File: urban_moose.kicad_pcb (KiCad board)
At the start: 2 copper layers, 27.4 x 49.5 mm, 52 parts, among them P1 SWD, P2 EXT, P3 ANT, Q1 MOSFET_N, Q2 MOSFET_N, SW1 SW_PUSH, U1 nRF51822-QFAA, U2 DS18B20, U3 BMP180, U4 Si1145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

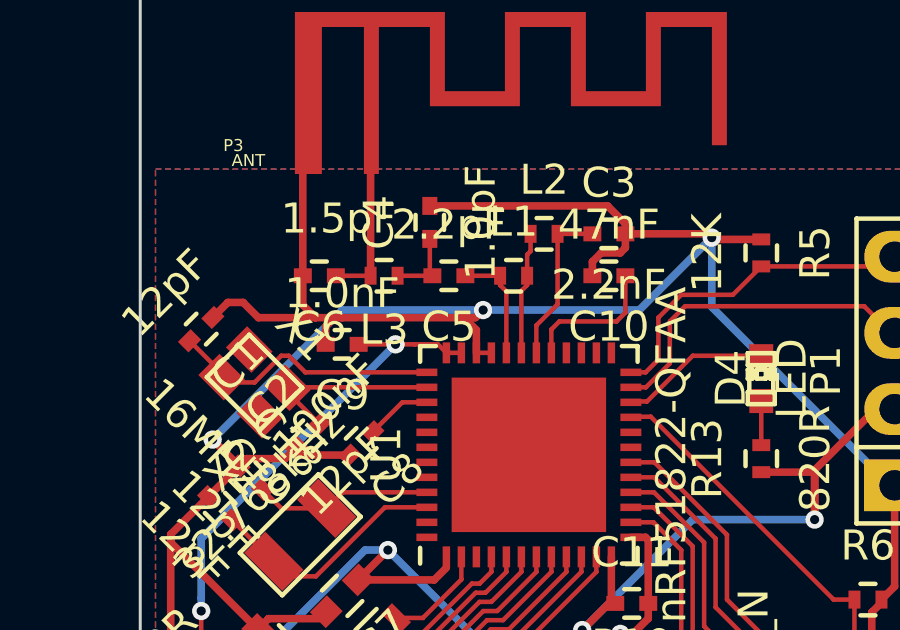
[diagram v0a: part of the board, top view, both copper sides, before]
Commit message: Ground vias added near matching components
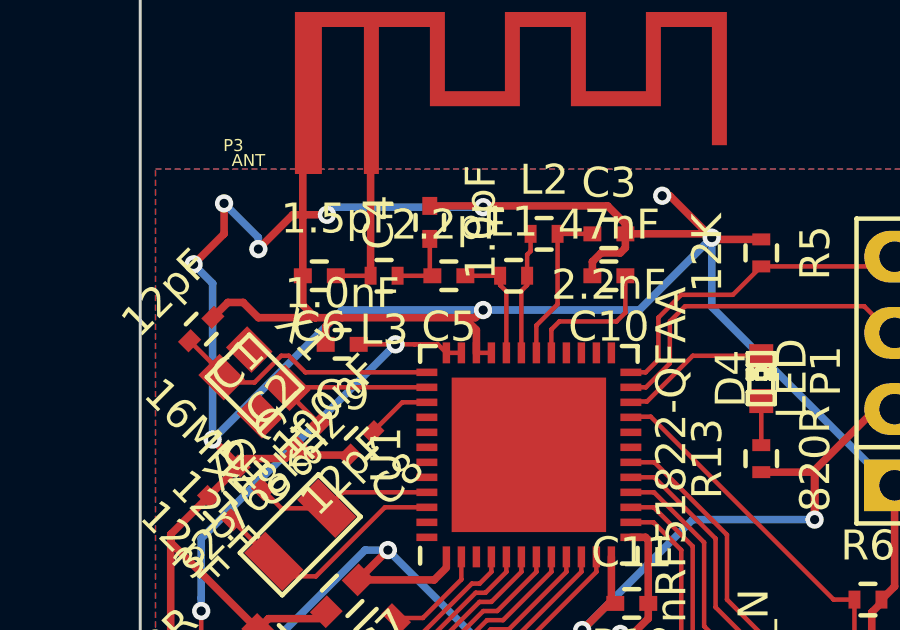
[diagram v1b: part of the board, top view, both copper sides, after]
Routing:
- net GND: track 236.2 -> 257.2 mm, vias 10 -> 16

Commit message: Tidy-ups
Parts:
- moved P3 54.2 mm to (137.9, 80.3)
- moved R9 53.8 mm to (141.1, 105.2)
- moved U1 53.8 mm to (145.3, 91.7)
- moved C1 53.8 mm to (134.4, 87.5)
- moved C11 53.8 mm to (148.7, 96.6)
- moved C13 53.8 mm to (143.0, 117.7)
- moved C14 53.8 mm to (151.9, 104.8)
- moved C17 53.8 mm to (135.3, 101.7)
- moved C18 53.8 mm to (136.0, 92.5)
- moved C3 53.8 mm to (148.0, 84.3)
- moved C4 53.8 mm to (142.0, 83.9)
- moved C5 53.8 mm to (142.6, 85.7)
- moved C8 53.8 mm to (139.7, 91.3)
- moved D2 53.8 mm to (156.5, 104.0)
- moved L2 53.8 mm to (145.8, 84.3)
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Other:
- board text added: "timhawes.com/um1"

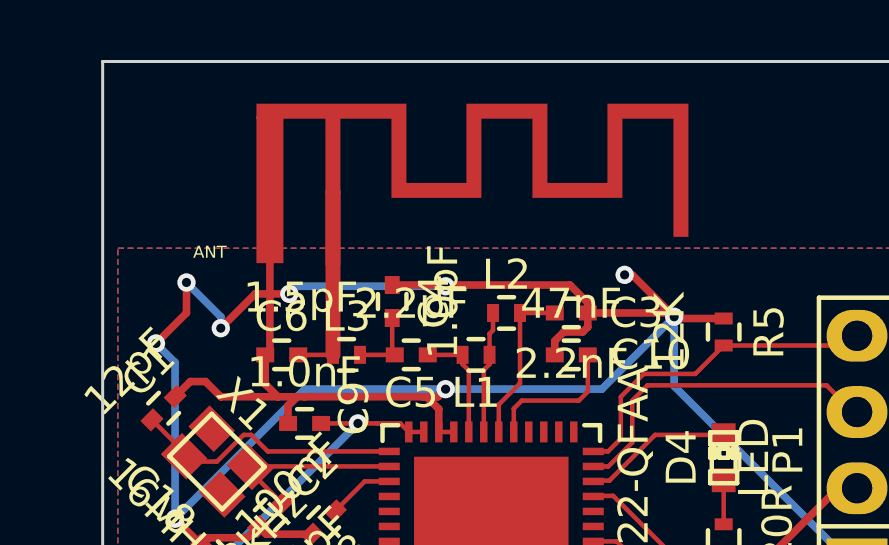
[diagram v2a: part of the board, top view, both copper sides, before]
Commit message: Move antenna away from ground plane
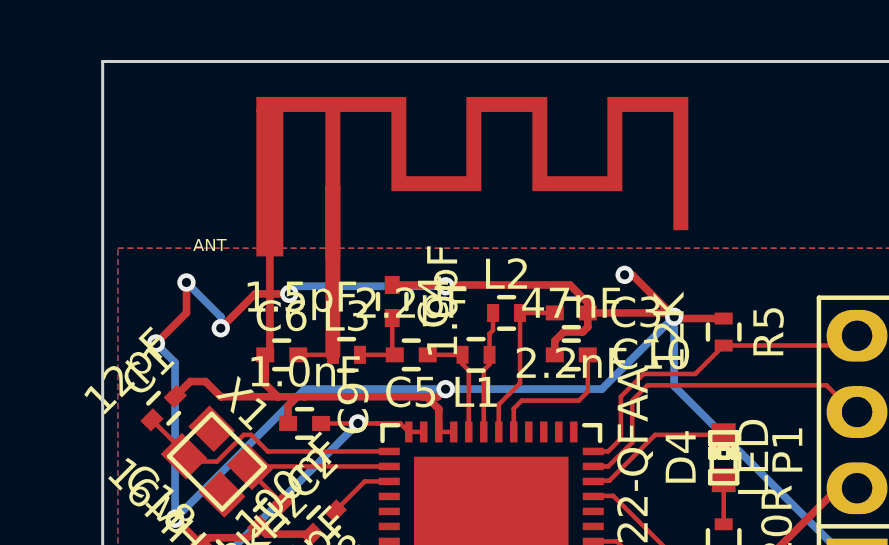
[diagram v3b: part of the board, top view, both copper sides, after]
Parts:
- moved P3 0.22 mm to (137.9, 80.1)
